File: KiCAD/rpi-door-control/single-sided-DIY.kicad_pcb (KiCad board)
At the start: 2 copper layers, 123 x 50 mm, 30 parts, among them IC1 4N35, J1 RJ45, P1 CONN_13X2, P2 CONN_2, P3 CONN_2, P4 CONN_2, Q1 2N3904, Q2 2N3904, SW1 SW_PUSH, U1 RELAY

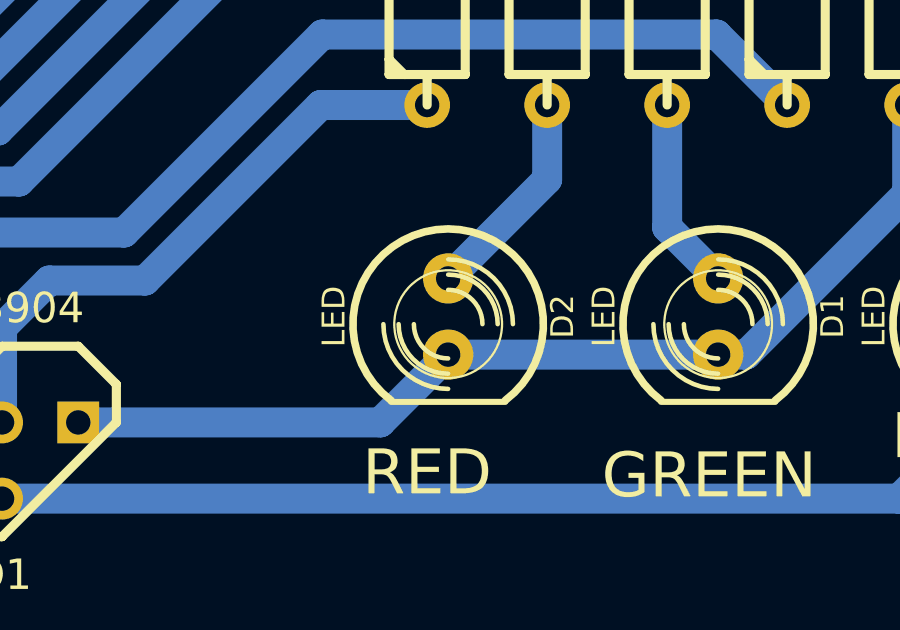
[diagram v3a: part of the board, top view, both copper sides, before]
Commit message: Changed the RED, DOOR and +12V LEDs to red
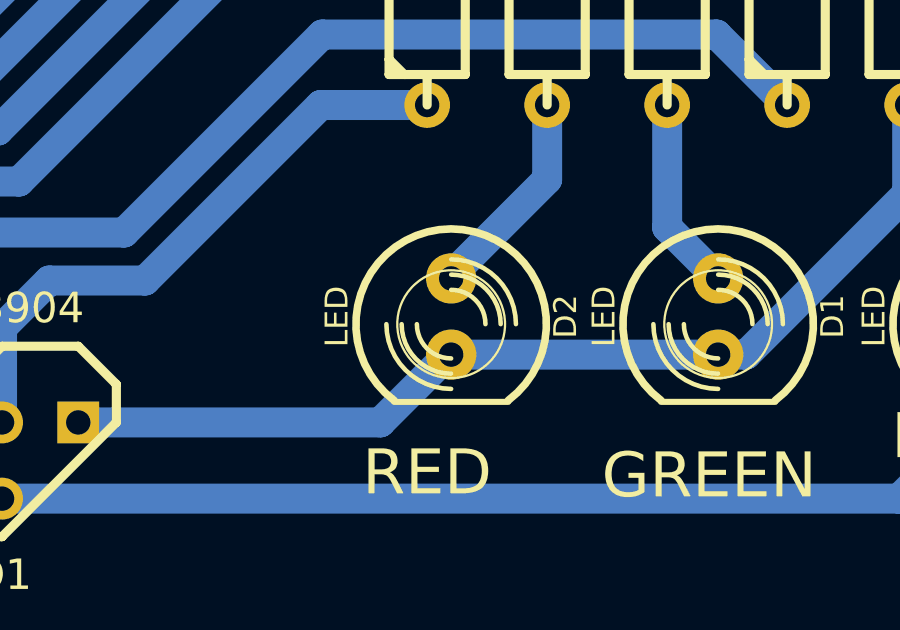
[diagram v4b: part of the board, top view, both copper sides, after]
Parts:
- D2, D3, D4: footprint LED-5MM -> LED-5MM-RED
- moved D2 0.10 mm to (128.4, 115.0)
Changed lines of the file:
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@@
-    )
-  )
-  (module LED-5MM (layer F.Cu)
-    (at 194.4 83 270)
-    (descr "LED 5mm - Lead pitch 100mil (2,54mm)")
-    (tags "LED led 5mm 5MM 100mil 2,54mm")
-    (fp_text reference D4 (at 0 -3.81 270) (layer F.SilkS)
-      (effects (font (size 0.762 0.762) (thickness 0.0889)))
-    )
-    (fp_text value LED (at 0 3.81 270) (layer F.SilkS)
-      (effects (font (size 0.762 0.762) (thickness 0.0889)))
-    )
-    (fp_line (start 2.8448 1.905) (end 2.8448 -1.905) (layer F.SilkS) (width 0.2032))
-    (fp_circle (center 0.254 0) (end -1.016 1.27) (layer F.SilkS) (width 0.0762))
-    (fp_arc (start 0.254 0) (end 2.794 1.905) (angle 286.2) (layer F.SilkS) (width 0.254))
-    (fp_arc (start 0.254 0) (end -0.889 0) (angle 90) (layer F.SilkS) (width 0.1524))
-    (fp_arc (start 0.254 0) (end 1.397 0) (angle 90) (layer F.SilkS) (width 0.1524))
-    (fp_arc (start 0.254 0) (end -1.397 0) (angle 90) (layer F.SilkS) (width 0.1524))
-    (fp_arc (start 0.254 0) (end 1.905 0) (angle 90) (layer F.SilkS) (width 0.1524))
-    (fp_arc (start 0.254 0) (end -1.905 0) (angle 90) (layer F.SilkS) (width 0.1524))
-    (fp_arc (start 0.254 0) (end 2.413 0) (angle 90) (layer F.SilkS) (width 0.1524))
-    (pad 1 thru_hole circle (at -1.27 0 270) (size 1.6764 1.6764) (drill 0.8128)
-      (layers *.Cu *.Mask F.SilkS)
-      (net 18 N-0000021)
-    )
-    (pad 2 thru_hole circle (at 1.27 0 270) (size 1.6764 1.6764) (drill 0.8128)
-      (layers *.Cu *.Mask F.SilkS)
-      (net 12 GNDPWR)
-    )
-    (model discret/leds/led5_vertical_verde.wrl
-      (at (xyz 0 0 0))
-      (scale (xyz 1 1 1))
-      (rotate (xyz 0 0 0))
-    )
-  )
-  (module LED-5MM (layer F.Cu)
-    (at 128.3 115 270)
-    (descr "LED 5mm - Lead pitch 100mil (2,54mm)")
-    (tags "LED led 5mm 5MM 100mil 2,54mm")
-    (fp_text reference D2 (at 0 -3.81 270) (layer F.SilkS)
-      (effects (font (size 0.762 0.762) (thickness 0.0889)))
-    )
-    (fp_text value LED (at 0 3.81 270) (layer F.SilkS)
-      (effects (font (size 0.762 0.762) (thickness 0.0889)))
-    )
-    (fp_line (start 2.8448 1.905) (end 2.8448 -1.905) (layer F.SilkS) (width 0.2032))
-    (fp_circle (center 0.254 0) (end -1.016 1.27) (layer F.SilkS) (width 0.0762))
-    (fp_arc (start 0.254 0) (end 2.794 1.905) (angle 286.2) (layer F.SilkS) (width 0.254))
-    (fp_arc (start 0.254 0) (end -0.889 0) (angle 90) (layer F.SilkS) (width 0.1524))
-    (fp_arc (start 0.254 0) (end 1.397 0) (angle 90) (layer F.SilkS) (width 0.1524))
-    (fp_arc (start 0.254 0) (end -1.397 0) (angle 90) (layer F.SilkS) (width 0.1524))
-    (fp_arc (start 0.254 0) (end 1.905 0) (angle 90) (layer F.SilkS) (width 0.1524))
-    (fp_arc (start 0.254 0) (end -1.905 0) (angle 90) (layer F.SilkS) (width 0.1524))
-    (fp_arc (start 0.254 0) (end 2.413 0) (angle 90) (layer F.SilkS) (width 0.1524))
-    (pad 1 thru_hole circle (at -1.27 0 270) (size 1.6764 1.6764) (drill 0.8128)
-      (layers *.Cu *.Mask F.SilkS)
-      (net 13 N-000001)
-    )
-    (pad 2 thru_hole circle (at 1.27 0 270) (size 1.6764 1.6764) (drill 0.8128)
-      (layers *.Cu *.Mask F.SilkS)
-      (net 11 GND)
-    )
-    (model discret/leds/led5_vertical_verde.wrl
-      (at (xyz 0 0 0))
-      (scale (xyz 1 1 1))
-      (rotate (xyz 0 0 0))
-    )
-  )
-  (module LED-5MM (layer F.Cu)
-    (at 146.3 115 270)
-    (descr "LED 5mm - Lead pitch 100mil (2,54mm)")
-    (tags "LED led 5mm 5MM 100mil 2,54mm")
-    (fp_text reference D3 (at 0 -3.81 270) (layer F.SilkS)
-      (effects (font (size 0.762 0.762) (thickness 0.0889)))
-    )
-    (fp_text value LED (at 0 3.81 270) (layer F.SilkS)
-      (effects (font (size 0.762 0.762) (thickness 0.0889)))
-    )
-    (fp_line (start 2.8448 1.905) (end 2.8448 -1.905) (layer F.SilkS) (width 0.2032))
-    (fp_circle (center 0.254 0) (end -1.016 1.27) (layer F.SilkS) (width 0.0762))
-    (fp_arc (start 0.254 0) (end 2.794 1.905) (angle 286.2) (layer F.SilkS) (width 0.254))
-    (fp_arc (start 0.254 0) (end -0.889 0) (angle 90) (layer F.SilkS) (width 0.1524))
-    (fp_arc (start 0.254 0) (end 1.397 0) (angle 90) (layer F.SilkS) (width 0.1524))
-    (fp_arc (start 0.254 0) (end -1.397 0) (angle 90) (layer F.SilkS) (width 0.1524))
-    (fp_arc (start 0.254 0) (end 1.905 0) (angle 90) (layer F.SilkS) (width 0.1524))
-    (fp_arc (start 0.254 0) (end -1.905 0) (angle 90) (layer F.SilkS) (width 0.1524))
-    (fp_arc (start 0.254 0) (end 2.413 0) (angle 90) (layer F.SilkS) (width 0.1524))
-    (pad 1 thru_hole circle (at -1.27 0 270) (size 1.6764 1.6764) (drill 0.8128)
-      (layers *.Cu *.Mask F.SilkS)
-      (net 20 N-0000026)
-    )
-    (pad 2 thru_hole circle (at 1.27 0 270) (size 1.6764 1.6764) (drill 0.8128)
-      (layers *.Cu *.Mask F.SilkS)
-      (net 19 N-0000025)
-    )
-    (model discret/leds/led5_vertical_verde.wrl
-      (at (xyz 0 0 0))
-      (scale (xyz 1 1 1))
-      (rotate (xyz 0 0 0))
     )
   )
@@
       (rotate (xyz 0 0 0))
     )
+  )
+  (module LED-5MM-RED (layer F.Cu)
+    (at 194.4 83 270)
+    (descr "LED 5mm - Lead pitch 100mil (2,54mm)")
+    (tags "LED led 5mm 5MM 100mil 2,54mm")
+    (fp_text reference D4 (at 0 -3.81 270) (layer F.SilkS)
+      (effects (font (size 0.762 0.762) (thickness 0.0889)))
+    )
+    (fp_text value LED (at 0 3.81 270) (layer F.SilkS)
+      (effects (font (size 0.762 0.762) (thickness 0.0889)))
+    )
+    (fp_line (start 2.8448 1.905) (end 2.8448 -1.905) (layer F.SilkS) (width 0.2032))
+    (fp_circle (center 0.254 0) (end -1.016 1.27) (layer F.SilkS) (width 0.0762))
+    (fp_arc (start 0.254 0) (end 2.794 1.905) (angle 286.2) (layer F.SilkS) (width 0.254))
+    (fp_arc (start 0.254 0) (end -0.889 0) (angle 90) (layer F.SilkS) (width 0.1524))
+    (fp_arc (start 0.254 0) (end 1.397 0) (angle 90) (layer F.SilkS) (width 0.1524))
+    (fp_arc (start 0.254 0) (end -1.397 0) (angle 90) (layer F.SilkS) (width 0.1524))
+    (fp_arc (start 0.254 0) (end 1.905 0) (angle 90) (layer F.SilkS) (width 0.1524))
+    (fp_arc (start 0.254 0) (end -1.905 0) (angle 90) (layer F.SilkS) (width 0.1524))
+    (fp_arc (start 0.254 0) (end 2.413 0) (angle 90) (layer F.SilkS) (width 0.1524))
+    (pad 1 thru_hole circle (at -1.27 0 270) (size 1.6764 1.6764) (drill 0.8128)
+      (layers *.Cu *.Mask F.SilkS)
+      (net 18 N-0000021)
+    )
+    (pad 2 thru_hole circle (at 1.27 0 270) (size 1.6764 1.6764) (drill 0.8128)
+      (layers *.Cu *.Mask F.SilkS)
+      (net 12 GNDPWR)
+    )
+    (model 3D_models/led5_vertical_red.wrl
+      (at (xyz 0 0 0))
+      (scale (xyz 1 1 1))
+      (rotate (xyz 0 0 0))
+    )
+  )
+  (module LED-5MM-RED (layer F.Cu)
+    (at 146.3 115 270)
+    (descr "LED 5mm - Lead pitch 100mil (2,54mm)")
+    (tags "LED led 5mm 5MM 100mil 2,54mm")
+    (fp_text reference D3 (at 0 -3.81 270) (layer F.SilkS)
+      (effects (font (size 0.762 0.762) (thickness 0.0889)))
+    )
+    (fp_text value LED (at 0 3.81 270) (layer F.SilkS)
+      (effects (font (size 0.762 0.762) (thickness 0.0889)))
+    )
+    (fp_line (start 2.8448 1.905) (end 2.8448 -1.905) (layer F.SilkS) (width 0.2032))
+    (fp_circle (center 0.254 0) (end -1.016 1.27) (layer F.SilkS) (width 0.0762))
+    (fp_arc (start 0.254 0) (end 2.794 1.905) (angle 286.2) (layer F.SilkS) (width 0.254))
+    (fp_arc (start 0.254 0) (end -0.889 0) (angle 90) (layer F.SilkS) (width 0.1524))
+    (fp_arc (start 0.254 0) (end 1.397 0) (angle 90) (layer F.SilkS) (width 0.1524))
+    (fp_arc (start 0.254 0) (end -1.397 0) (angle 90) (layer F.SilkS) (width 0.1524))
+    (fp_arc (start 0.254 0) (end 1.905 0) (angle 90) (layer F.SilkS) (width 0.1524))
+    (fp_arc (start 0.254 0) (end -1.905 0) (angle 90) (layer F.SilkS) (width 0.1524))
+    (fp_arc (start 0.254 0) (end 2.413 0) (angle 90) (layer F.SilkS) (width 0.1524))
+    (pad 1 thru_hole circle (at -1.27 0 270) (size 1.6764 1.6764) (drill 0.8128)
+      (layers *.Cu *.Mask F.SilkS)
+      (net 20 N-0000026)
+    )
+    (pad 2 thru_hole circle (at 1.27 0 270) (size 1.6764 1.6764) (drill 0.8128)
+      (layers *.Cu *.Mask F.SilkS)
+      (net 19 N-0000025)
+    )
+    (model 3D_models/led5_vertical_red.wrl
+      (at (xyz 0 0 0))
+      (scale (xyz 1 1 1))
+      (rotate (xyz 0 0 0))
+    )
+  )
+  (module LED-5MM-RED (layer F.Cu)
+    (at 128.4 115 270)
+    (descr "LED 5mm - Lead pitch 100mil (2,54mm)")
+    (tags "LED led 5mm 5MM 100mil 2,54mm")
+    (fp_text reference D2 (at 0 -3.81 270) (layer F.SilkS)
+      (effects (font (size 0.762 0.762) (thickness 0.0889)))
+    )
+    (fp_text value LED (at 0 3.81 270) (layer F.SilkS)
+      (effects (font (size 0.762 0.762) (thickness 0.0889)))
+    )
+    (fp_line (start 2.8448 1.905) (end 2.8448 -1.905) (layer F.SilkS) (width 0.2032))
+    (fp_circle (center 0.254 0) (end -1.016 1.27) (layer F.SilkS) (width 0.0762))
+    (fp_arc (start 0.254 0) (end 2.794 1.905) (angle 286.2) (layer F.SilkS) (width 0.254))
+    (fp_arc (start 0.254 0) (end -0.889 0) (angle 90) (layer F.SilkS) (width 0.1524))
+    (fp_arc (start 0.254 0) (end 1.397 0) (angle 90) (layer F.SilkS) (width 0.1524))
+    (fp_arc (start 0.254 0) (end -1.397 0) (angle 90) (layer F.SilkS) (width 0.1524))
+    (fp_arc (start 0.254 0) (end 1.905 0) (angle 90) (layer F.SilkS) (width 0.1524))
+    (fp_arc (start 0.254 0) (end -1.905 0) (angle 90) (layer F.SilkS) (width 0.1524))
+    (fp_arc (start 0.254 0) (end 2.413 0) (angle 90) (layer F.SilkS) (width 0.1524))
+    (pad 1 thru_hole circle (at -1.27 0 270) (size 1.6764 1.6764) (drill 0.8128)
+      (layers *.Cu *.Mask F.SilkS)
+      (net 13 N-000001)
+    )
+    (pad 2 thru_hole circle (at 1.27 0 270) (size 1.6764 1.6764) (drill 0.8128)
+      (layers *.Cu *.Mask F.SilkS)
+      (net 11 GND)
+    )
+    (model 3D_models/led5_vertical_red.wrl
+      (at (xyz 0 0 0))
+      (scale (xyz 1 1 1))
+      (rotate (xyz 0 0 0))
+    )

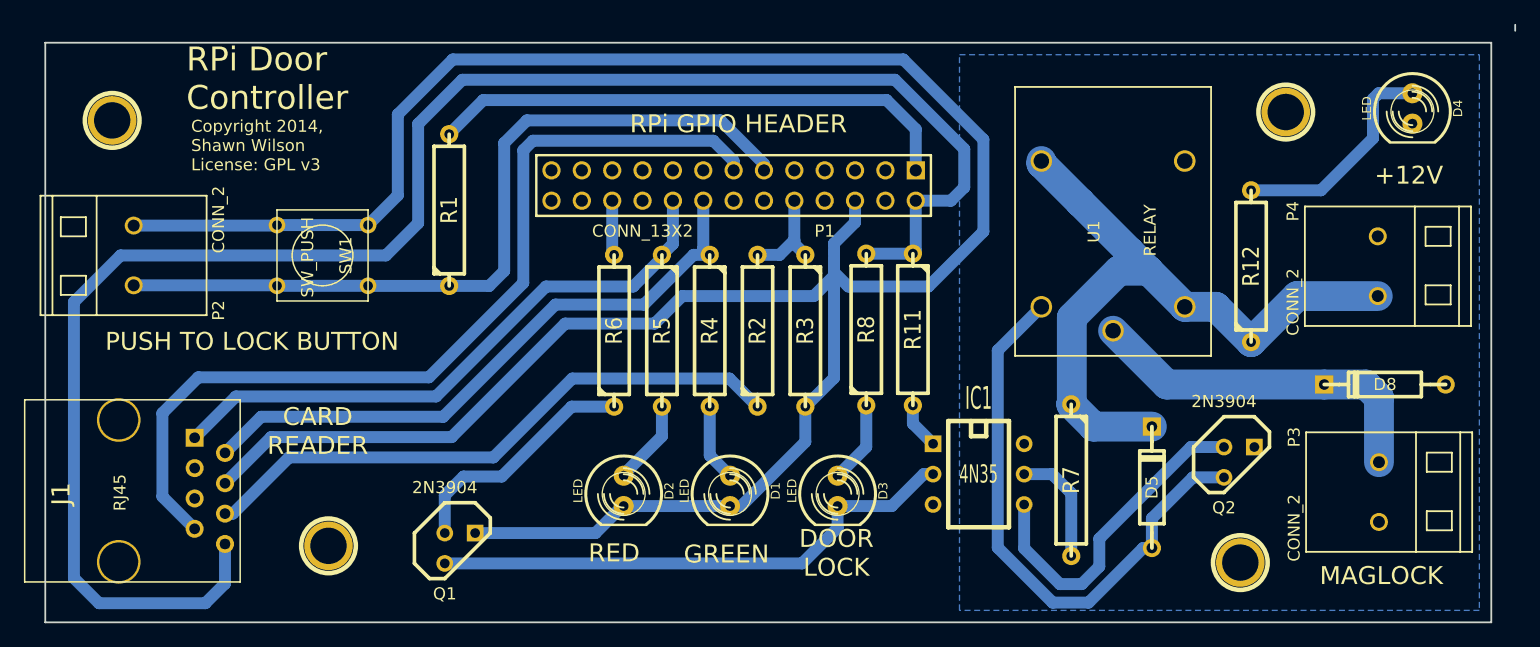
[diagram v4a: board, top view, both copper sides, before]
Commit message: Moved parts around on 12V side and aligned holes better
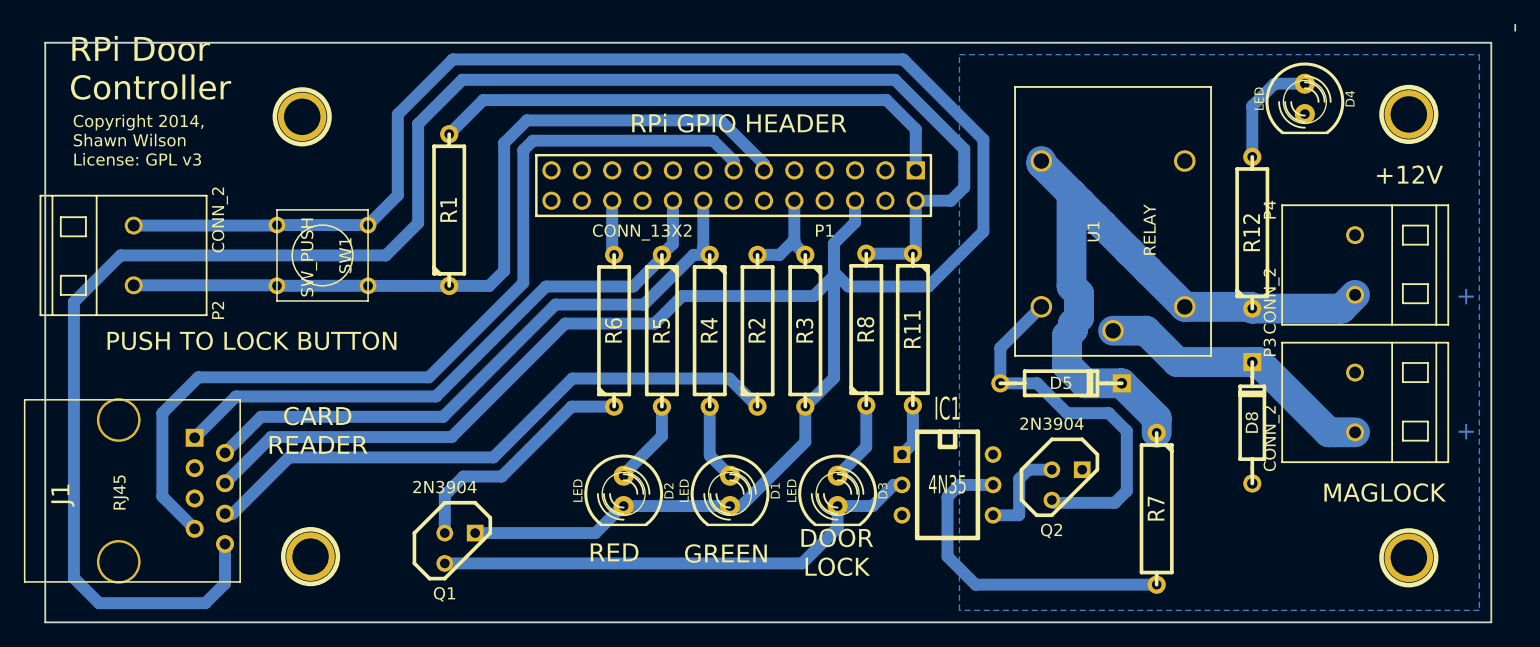
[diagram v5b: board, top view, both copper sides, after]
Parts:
- moved ? 15.9 mm to (101.5, 83.7)
- moved Q2 14.5 mm to (165.5, 114.5)
- moved ? 14.1 mm to (194.1, 120.6)
- moved D5 11.6 mm to (165.0, 106.0), turned to 0 degrees
- moved D8 11.6 mm to (181.0, 109.3), turned to 90 degrees
- moved ? 10.3 mm to (194.1, 83.5)
- moved D4 9.04 mm to (185.4, 82.2)
- moved P3 7.76 mm to (189.6, 107.6)
- moved R7 7.54 mm to (173.0, 116.5)
- moved R12 2.80 mm to (181.0, 93.4)
- moved IC1 2.75 mm to (155.5, 114.5)
- moved P4 1.90 mm to (189.6, 96.1)
- moved ? 1.75 mm to (102.2, 120.5)
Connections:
- P3 pad 1: N-0000027 -> GNDPWR
- P3 pad 2: GNDPWR -> N-0000027
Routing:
- net N-0000020: track 27.7 -> 8.26 mm
- net N-0000018: track 9.85 -> 27.7 mm
- net N-0000038: track 48.3 -> 31.8 mm
- net N-0000021: track 18.8 -> 9.42 mm
- net N-0000027: track 30.0 -> 23.8 mm
- net N-0000025: track 45.0 -> 42.1 mm
- net +12V: track 59.1 -> 57.6 mm
- net N-0000019: track 3.91 -> 4.49 mm
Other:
- board text added: "+"
